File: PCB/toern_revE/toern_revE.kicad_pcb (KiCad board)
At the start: 4 copper layers, 160 x 71 mm, 77 parts, among them J1 AudioJack3_Switch, J11 Conn_01x05, J11.5 Conn_01x05, J12 Conn_01x05, J13 Conn_01x05, J14 Conn_01x05, J15 Conn_01x05, J16 BATTERY, J2 CUI_SJ2-35863B1-SMT-TR, J3 CUI_SJ2-35863B1-SMT-TR, J4 USB_C_Receptacle_USB2.0, J5 AudioJack3_Switch, J6 AudioJack3_Switch, J7 AudioJack3_Switch, J8 Micro_SD_Card, J9 Conn_01x03, Q1 DMG3415, SW1 EG2219, U1 SPX3819M5-L-3-3, U10 01x05 Connector_PinSocket_2.5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, U11 01x05 Connector_PinSocket_2.5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, U12 01x05 Connector_PinSocket_2.5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, U2 SPX3819M5-L-1-8, U3 SGTL5000XNBA3, U4 TLP2361V4_E, U5 74LVC2G14, U6 Teensy4.1, U7 SPX3819M5-L-3-3, U8 MCP73831-3-OT, U9 01x05 Connector_PinSocket_2.5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

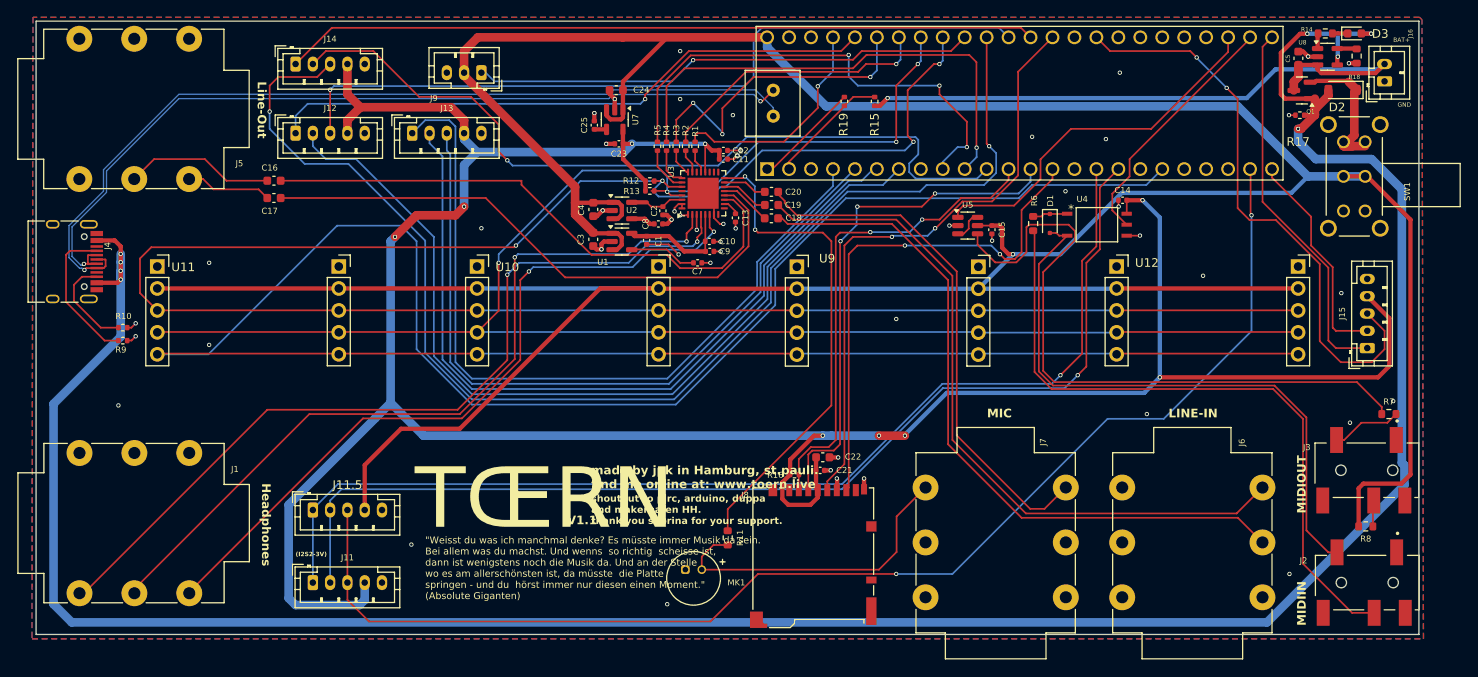
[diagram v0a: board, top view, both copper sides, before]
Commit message: varoious fixes in stability
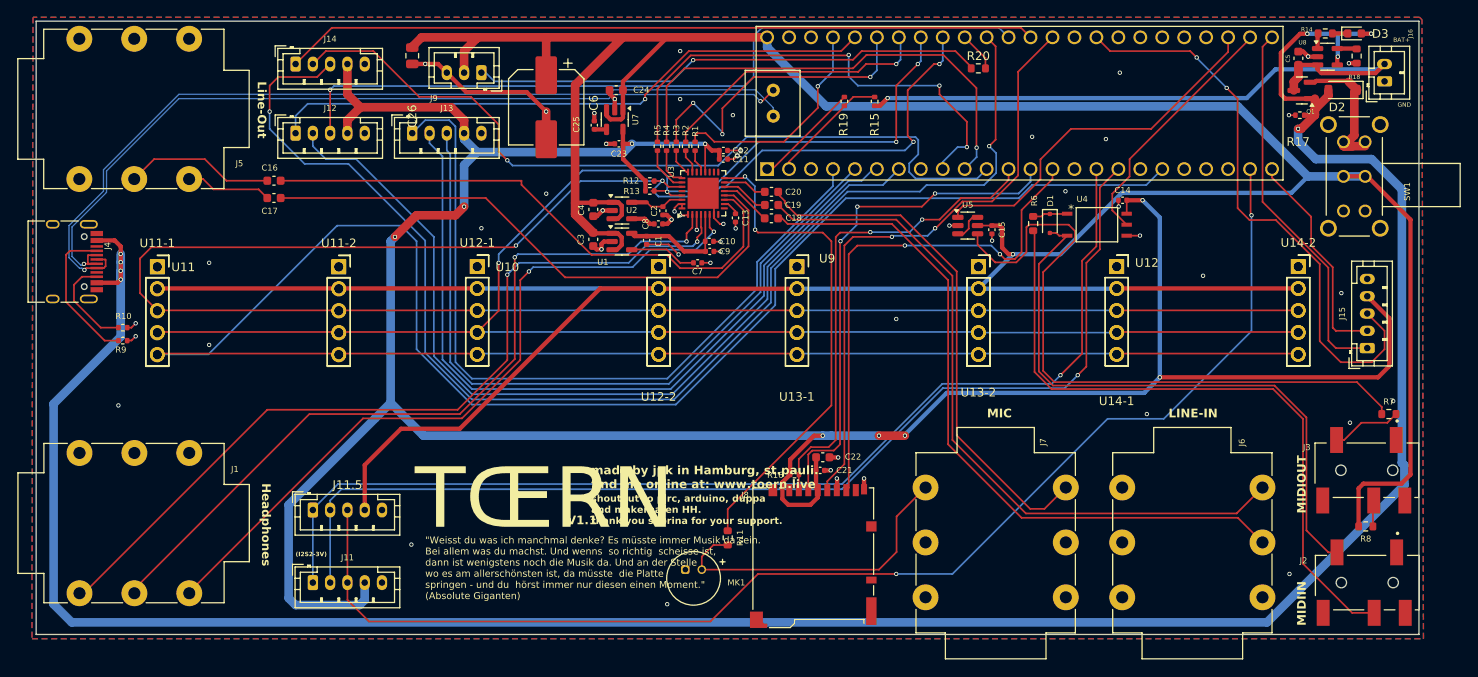
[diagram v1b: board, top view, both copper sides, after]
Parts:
- added C26: 100nF, Capacitor_SMD:C_0805_2012Metric, F.Cu at (74.5, 29.0)
- added C6: 1000uF, Capacitor_SMD:CP_Elec_8x10.5, F.Cu at (90.0, 35.0)
- added R20: 220R, Resistor_SMD:R_0603_1608Metric, F.Cu at (140.0, 30.5)
- added U11-1: PinSocket_1x05_P2.54mm_Vertical, Connector_PinSocket_2.54mm:PinSocket_1x05_P2.54mm_Vertical, F.Cu at (45.0, 53.5)
- added U11-2: PinSocket_1x05_P2.54mm_Vertical, Connector_PinSocket_2.54mm:PinSocket_1x05_P2.54mm_Vertical, F.Cu at (66.0, 53.5)
- added U12-1: PinSocket_1x05_P2.54mm_Vertical, Connector_PinSocket_2.54mm:PinSocket_1x05_P2.54mm_Vertical, F.Cu at (82.0, 53.5)
- added U12-2: PinSocket_1x05_P2.54mm_Vertical, Connector_PinSocket_2.54mm:PinSocket_1x05_P2.54mm_Vertical, F.Cu at (103.0, 53.5)
- added U13-1: PinSocket_1x05_P2.54mm_Vertical, Connector_PinSocket_2.54mm:PinSocket_1x05_P2.54mm_Vertical, F.Cu at (119.0, 53.5)
- added U13-2: PinSocket_1x05_P2.54mm_Vertical, Connector_PinSocket_2.54mm:PinSocket_1x05_P2.54mm_Vertical, F.Cu at (140.0, 53.5)
- added U14-1: PinSocket_1x05_P2.54mm_Vertical, Connector_PinSocket_2.54mm:PinSocket_1x05_P2.54mm_Vertical, F.Cu at (156.0, 53.5)
- added U14-2: PinSocket_1x05_P2.54mm_Vertical, Connector_PinSocket_2.54mm:PinSocket_1x05_P2.54mm_Vertical, F.Cu at (177.0, 53.5)
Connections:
- J9 pad 1: 17_A3_TX4_SDA1 -> Net-(J9-Pin_1)
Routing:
- net Net-(J9-Pin_1): track 0.00 -> 59.3 mm, vias 0 -> 1
- net 17_A3_TX4_SDA1: track 58.4 -> 4.66 mm, vias 1 -> 0
- net GND: track 60.1 -> 81.0 mm, vias 50 -> 53
- net +5V: track 459.7 -> 473.6 mm
- net 8_TX2_IN1: track 57.1 -> 55.3 mm
- net 16_A2_RX4_SCL1: track 147.0 -> 147.6 mm
